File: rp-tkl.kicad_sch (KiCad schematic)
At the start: 5 parts

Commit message: Finished most of preliminary schematic
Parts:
- added C?: 10uF, Capacitor_SMD:C_0402_1005Metric, symbol Device:C_Small
- added C? (x10): 100nF, Capacitor_SMD:C_0402_1005Metric, symbol Device:C_Small
- added C? (x4): 1uF, Capacitor_SMD:C_0402_1005Metric, symbol Device:C_Small
- added C? (x2): 22pF, Capacitor_SMD:C_0402_1005Metric, symbol Device:C_Small
- added F?: 500mA, Fuse:Fuse_1206_3216Metric, symbol Device:Polyfuse_Small
- added R? (x2): 1k, Resistor_SMD:R_0402_1005Metric, symbol Device:R_Small
- added R? (x2): 27R, Resistor_SMD:R_0603_1608Metric, symbol Device:R_Small
- added R? (x2): 5.1k, Resistor_SMD:R_0402_1005Metric, symbol Device:R_Small
- added R?: 10k, Resistor_SMD:R_0402_1005Metric, symbol Device:R_Small
- added SW?: SW_Push, Connector_PinSocket_2.54mm:PinSocket_1x02_P2.54mm_Vertical, symbol Switch:SW_Push
- added Y?: 12MHz, Crystal:Crystal_SMD_3225-4Pin_3.2x2.5mm, symbol Device:Crystal_GND24_Small
- J?: footprint (none) -> Connector_USB:USB_C_Receptacle_HRO_TYPE-C-31-M-12
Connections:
- net IOVDD is gone; now on net +3V3: U?.1 (IOVDD), U?.10 (IOVDD), U?.22 (IOVDD), U?.33 (IOVDD), U?.42 (IOVDD), U?.49 (IOVDD)
- net GND: now reaches U?.2 (VN)
- net GND: now also J?.A1 (GND), J?.A12 (GND), J?.B1 (GND), J?.B12 (GND), J?.S1 (SHIELD), U?.1 (GND), U?.19 (TESTEN), U?.4 (GND), U?.57 (GND), C?.1, C?.1, C?.1, C?.1, C?.2, C?.2, C?.2, C?.2, C?.2, C?.2, C?.2, C?.2, C?.2, C?.2, C?.2, C?.2, C?.2, R?.2, R?.2, SW?.1, Y?.2, Y?.4
- net DBUS-: now reaches U?.3 (IO2)
- net DBUS-: now also J?.A7 (D-), J?.B7 (D-), R?.1
- net DBUS+: now reaches U?.4 (IO3)
- net DBUS+: now also J?.A6 (D+), J?.B6 (D+), R?.1
- net +5V: now reaches U?.5 (VP)
- net +5V: now also U?.3 (VI), C?.2, F?.2
- net +3V3: now reaches U?.2 (VO)
- net +3V3: now also U?.43 (ADC_AVDD), U?.48 (USB_VDD), U?.8 (VCC), C?.1, C?.1, C?.1, C?.1, C?.1, C?.1, C?.1, C?.1, C?.1, C?.1, C?.2, R?.1
- net XTAL_IN: now reaches U?.20 (XTAL_IN)
- net XTAL_IN: now also C?.2, Y?.3
- net XTAL_OUT: now reaches U?.21 (XTAL_OUT)
- net XTAL_OUT: now also R?.2
- net SWCLK: now reaches U?.24 (SWCLK)
- net SWD: now reaches U?.25 (SWDIO)
- net ~{RESET}: now reaches U?.26 (~{RUN})
- net ~{RESET}: now also R?.2
- net D_-: now reaches U?.46 (D-)
- net D_-: now also R?.2
- net D_+: now reaches U?.47 (D+)
- net D_+: now also R?.2
- net SD3: now reaches U?.51 (QSPI_SD3)
- net SD3: now also U?.7 (IO3)
- net QSPI_CLK: now reaches U?.52 (QSPI_SCLK)
- net QSPI_CLK: now also U?.6 (CLK)
- net SD0: now reaches U?.53 (QSPI_SD0)
- net SD0: now also U?.5 (DI(IO0))
- net SD2: now reaches U?.54 (QSPI_SD2)
- net SD2: now also U?.3 (IO2)
- net SD1: now reaches U?.55 (QSPI_SD1)
- net SD1: now also U?.2 (DO(IO1))
- net CS: now reaches U?.56 (QSPI_SS_N)
- net CS: now also U?.1 (~{CS}), R?.2
- net VBUS: now reaches J?.A4 (VBUS), J?.A9 (VBUS), J?.B4 (VBUS), J?.B9 (VBUS)
- net VBUS: now also F?.1
- net CC1: now reaches J?.A5 (CC1)
- net CC1: now also R?.1
- net CC2: now reaches J?.B5 (CC2)
- net CC2: now also R?.1
- net DVDD renamed +1V1
- net +1V1: now also C?.1, C?.1, C?.1
- new net XTAL_O: C?.2, R?.1, Y?.1
- new net ~{USB_BOOT}: R?.1, SW?.2
- no-connect marks 0 -> 2
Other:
- moved on the sheet: J?, U?

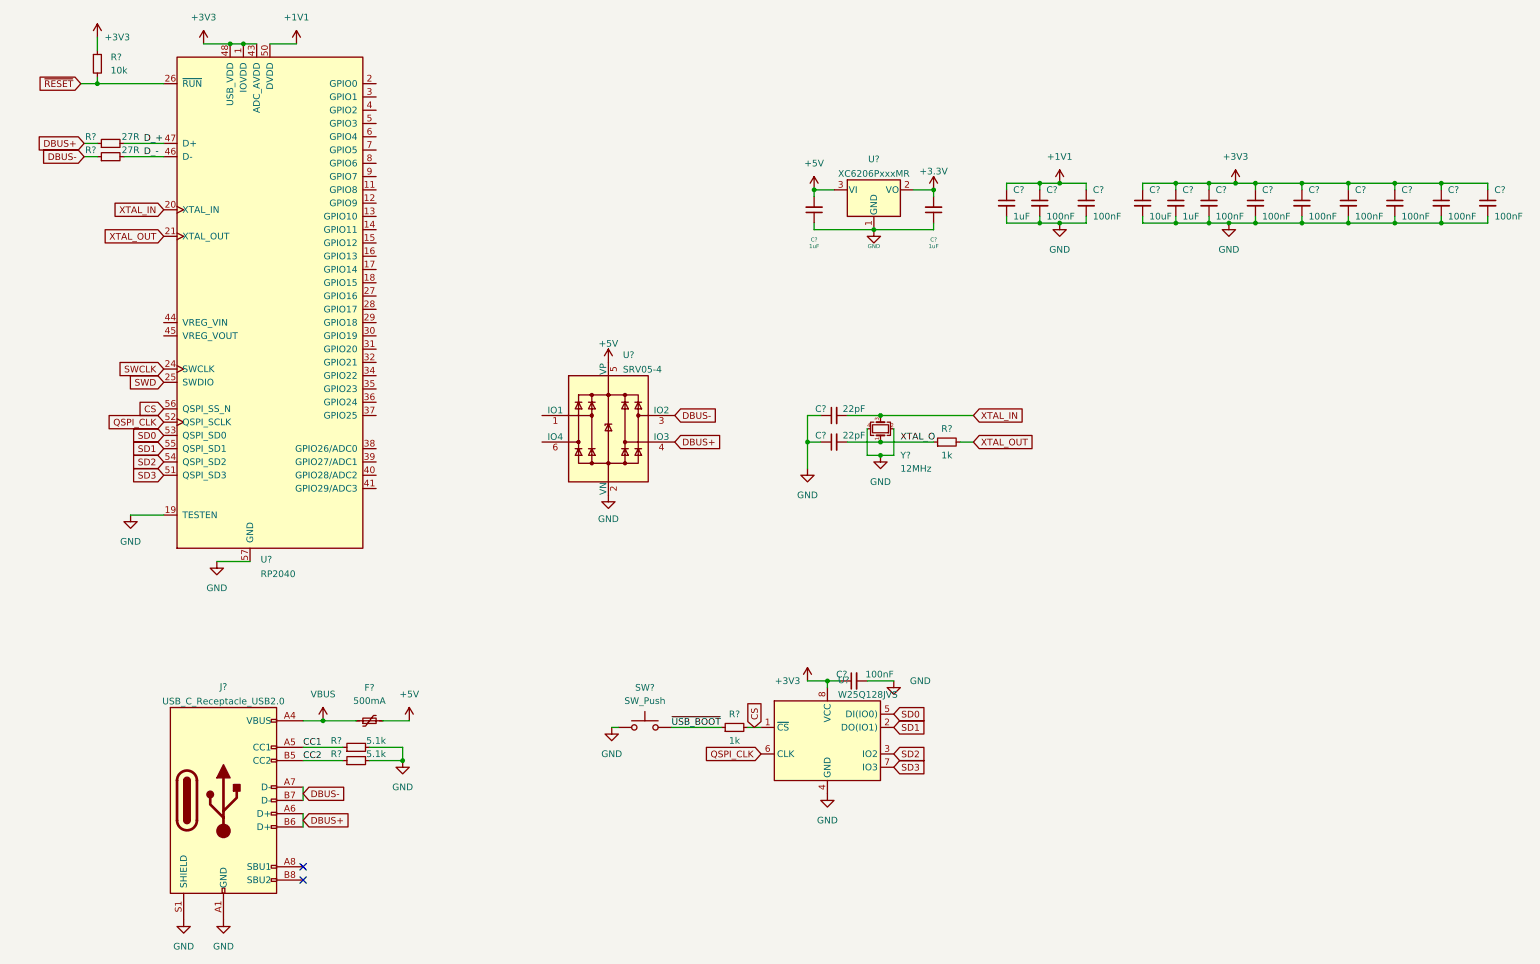
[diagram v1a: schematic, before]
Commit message: Added Footprint Libs, Annotated schematic, Imported footprints
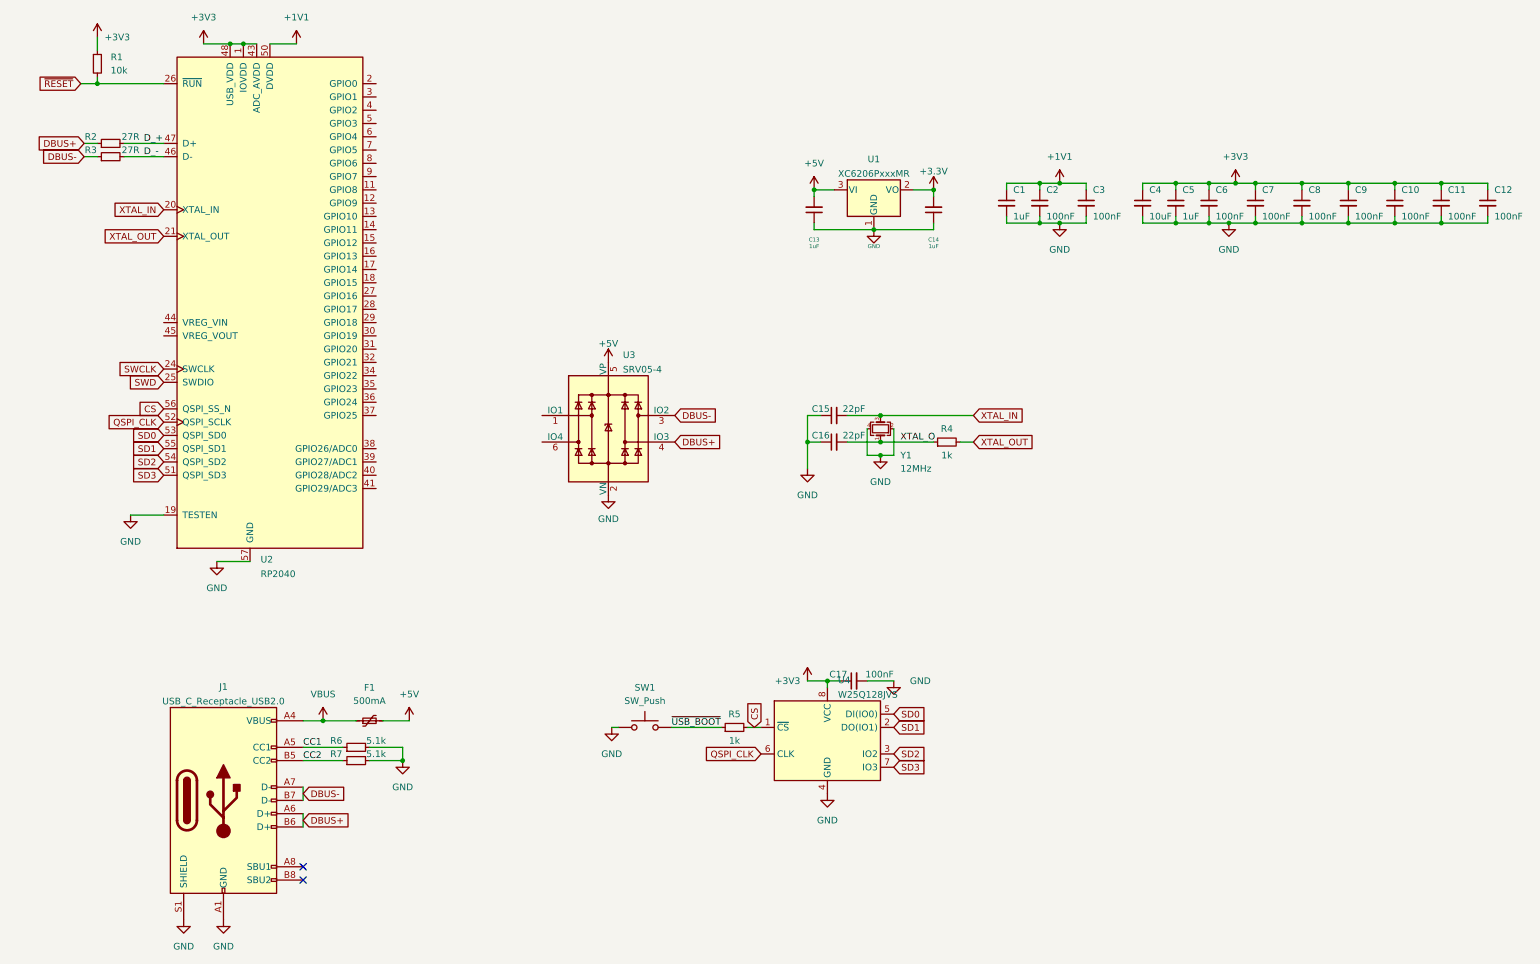
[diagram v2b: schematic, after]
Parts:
- U2: renamed from U?; footprint Sleep-Lib:RP2040-QFN-56 -> Sleep-lib:RP2040-QFN-56
- gave numbers to parts that had none: 31

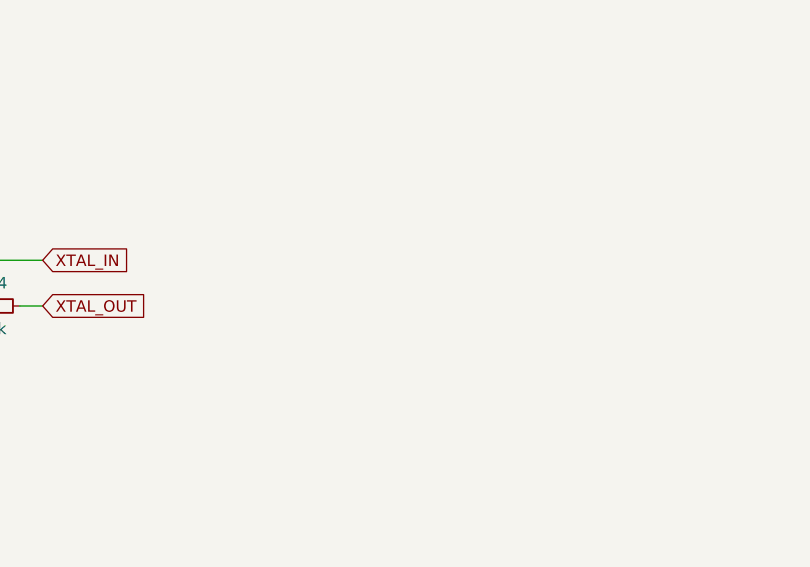
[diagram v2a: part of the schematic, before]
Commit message: [Excluding Switches] Moved components to rough positions on pcb
Also added 5 pin programming header
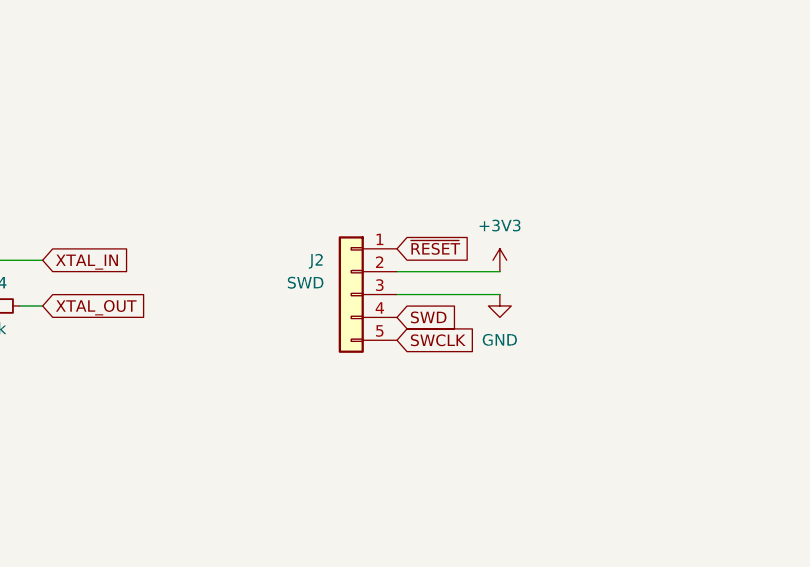
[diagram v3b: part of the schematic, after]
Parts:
- added J2: SWD, Connector_PinSocket_2.54mm:PinSocket_1x05_P2.54mm_Vertical, symbol Connector_Generic:Conn_01x05
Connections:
- net +3V3: now also J2.2 (Pin_2)
- net GND: now also J2.3 (Pin_3)
- net SWCLK: now also J2.5 (Pin_5)
- net SWD: now also J2.4 (Pin_4)
- net ~{RESET}: now also J2.1 (Pin_1)
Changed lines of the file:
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@@
+    (stroke (width 0) (type default) (color 0 0 0 0))
+  )
+  (wire (pts (xy 240.03 114.3) (xy 251.46 114.3))
     (stroke (width 0) (type default) (color 0 0 0 0))
   )
@@
   )
   (wire (pts (xy 72.39 189.23) (xy 72.39 191.77))
+    (stroke (width 0) (type default) (color 0 0 0 0))
+  )
+  (wire (pts (xy 251.46 116.84) (xy 240.03 116.84))
     (stroke (width 0) (type default) (color 0 0 0 0))
   )
@@
     )
   )
+  (global_label "SWD" (shape input) (at 240.03 119.38 0) (fields_autoplaced)
+    (effects (font (size 1.27 1.27)) (justify left))
+    (property "Intersheet References" "${INTERSHEET_REFS}" (id 0) (at 246.3741 119.3006 0)
+      (effects (font (size 1.27 1.27)) (justify left) hide)
+    )
+  )
   (global_label "SWD" (shape input) (at 45.72 106.68 180) (fields_autoplaced)
     (effects (font (size 1.27 1.27)) (justify right))
@@
     )
   )
+  (global_label "SWCLK" (shape input) (at 240.03 121.92 0) (fields_autoplaced)
+    (effects (font (size 1.27 1.27)) (justify left))
+    (property "Intersheet References" "${INTERSHEET_REFS}" (id 0) (at 248.6721 121.8406 0)
+      (effects (font (size 1.27 1.27)) (justify left) hide)
+    )
+  )
   (global_label "SD2" (shape input) (at 45.72 121.92 180) (fields_autoplaced)
     (effects (font (size 1.27 1.27)) (justify right))
@@
     )
   )
+  (global_label "~{RESET}" (shape input) (at 240.03 111.76 0) (fields_autoplaced)
+    (effects (font (size 1.27 1.27)) (justify left))
+    (property "Intersheet References" "${INTERSHEET_REFS}" (id 0) (at 248.1883 111.6806 0)
+      (effects (font (size 1.27 1.27)) (justify left) hide)
+    )
+  )
   (global_label "SD0" (shape input) (at 45.72 116.84 180) (fields_autoplaced)
     (effects (font (size 1.27 1.27)) (justify right))
@@
     (pin "2")
   )
+  (symbol (lib_id "power:+3V3") (at 251.46 114.3 0) (unit 1)
+    (in_bom yes) (on_board yes) (fields_autoplaced)
+    (property "Reference" "#PWR026" (id 0) (at 251.46 118.11 0)
+      (effects (font (size 1.27 1.27)) hide)
+    )
+    (property "Value" "+3V3" (id 1) (at 251.46 109.22 0))
+    (property "Footprint" "" (id 2) (at 251.46 114.3 0)
+      (effects (font (size 1.27 1.27)) hide)
+    )
+    (property "Datasheet" "" (id 3) (at 251.46 114.3 0)
+      (effects (font (size 1.27 1.27)) hide)
+    )
+    (pin "1")
+  )
   (symbol (lib_id "power:GND") (at 91.44 179.07 0) (unit 1)
     (in_bom yes) (on_board yes) (fields_autoplaced)
@@
     (pin "1")
     (pin "2")
+  )
+  (symbol (lib_id "Connector_Generic:Conn_01x05") (at 234.95 116.84 0) (mirror y) (unit 1)
+    (in_bom no) (on_board yes)
+    (property "Reference" "J2" (id 0) (at 231.14 113.03 0))
+    (property "Value" "SWD" (id 1) (at 229.87 115.57 0))
+    (property "Footprint" "Connector_PinSocket_2.54mm:PinSocket_1x05_P2.54mm_Vertical" (id 2) (at 234.95 116.84 0)
+      (effects (font (size 1.27 1.27)) hide)
+    )
+    (property "Datasheet" "~" (id 3) (at 234.95 116.84 0)
+      (effects (font (size 1.27 1.27)) hide)
+    )
+    (pin "1")
+    (pin "2")
+    (pin "3")
+    (pin "4")
+    (pin "5")
   )
   (symbol (lib_id "power:+3V3") (at 168.91 163.83 0) (unit 1)
@@
     (pin "1")
   )
+  (symbol (lib_id "power:GND") (at 251.46 116.84 0) (unit 1)
+    (in_bom yes) (on_board yes) (fields_autoplaced)
+    (property "Reference" "#PWR027" (id 0) (at 251.46 123.19 0)
+      (effects (font (size 1.27 1.27)) hide)
+    )
+    (property "Value" "GND" (id 1) (at 251.46 121.92 0))
+    (property "Footprint" "" (id 2) (at 251.46 116.84 0)
+      (effects (font (size 1.27 1.27)) hide)
+    )
+    (property "Datasheet" "" (id 3) (at 251.46 116.84 0)
+      (effects (font (size 1.27 1.27)) hide)
+    )
+    (pin "1")
+  )
   (symbol (lib_id "Device:C_Small") (at 170.18 73.66 180) (unit 1)
     (in_bom yes) (on_board yes)
@@
       (reference "#PWR025") (unit 1) (value "GND") (footprint "")
     )
+    (path "/314fa90a-4b52-4c8b-9d5d-a2a2fca67558"
+      (reference "#PWR026") (unit 1) (value "+3V3") (footprint "")
+    )
+    (path "/e926f35f-3f27-4b2d-80bf-c5ceafb83f8e"
+      (reference "#PWR027") (unit 1) (value "GND") (footprint "")
+    )
     (path "/29f11a32-f398-46d6-95a0-57f3be58392e"
       (reference "C1") (unit 1) (value "1uF") (footprint "Capacitor_SMD:C_0402_1005Metric")
@@
       (reference "J1") (unit 1) (value "USB_C_Receptacle_USB2.0") (footprint "Connector_USB:USB_C_Receptacle_HRO_TYPE-C-31-M-12")
     )
+    (path "/488e1dfc-da13-4e5c-9edf-756b09e35c04"
+      (reference "J2") (unit 1) (value "SWD") (footprint "Connector_PinSocket_2.54mm:PinSocket_1x05_P2.54mm_Vertical")
+    )
     (path "/d5f64c48-5769-4554-8a1d-d23f7b2152b1"

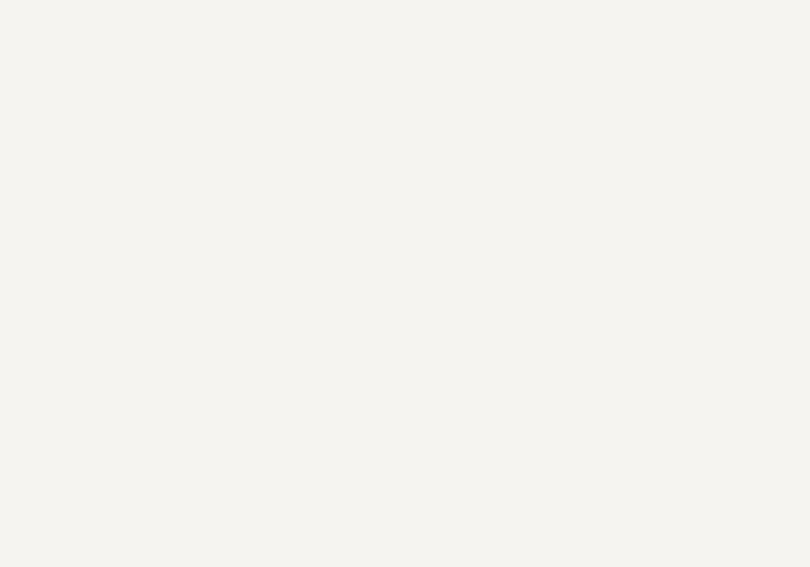
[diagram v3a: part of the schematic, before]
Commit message: [Preliminary] Added Switch matrix and imported footprints
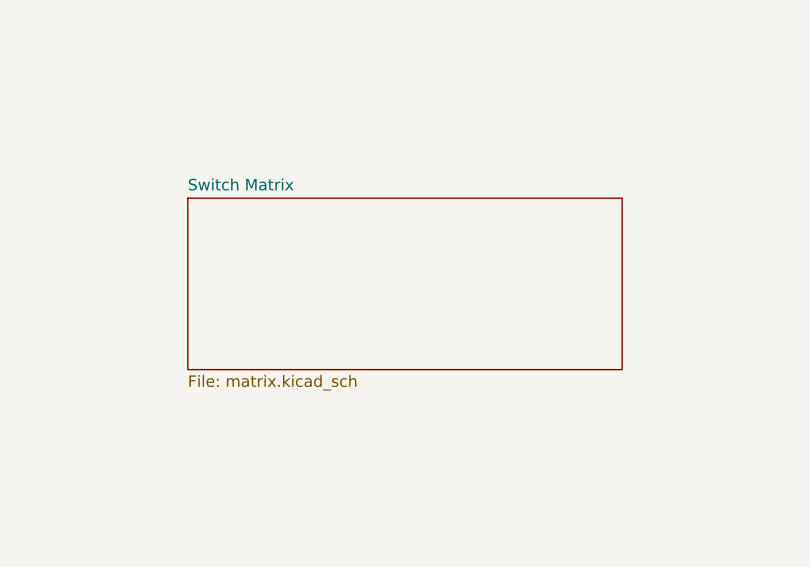
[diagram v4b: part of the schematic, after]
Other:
- added sheet Switch Matrix (matrix.kicad_sch)

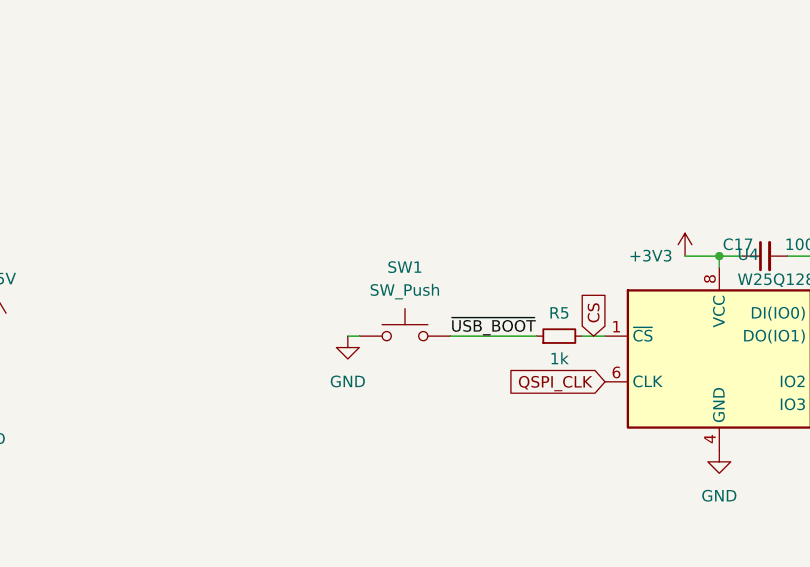
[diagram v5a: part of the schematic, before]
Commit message: All switches (not diodes) in position
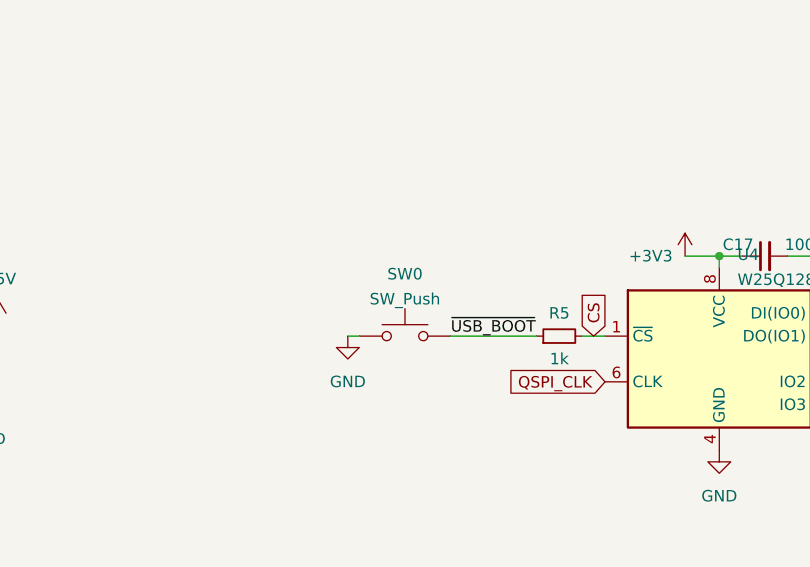
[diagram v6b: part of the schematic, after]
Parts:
- renumbered SW1 to SW0
